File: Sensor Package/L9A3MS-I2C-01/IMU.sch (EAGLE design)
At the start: 15 parts

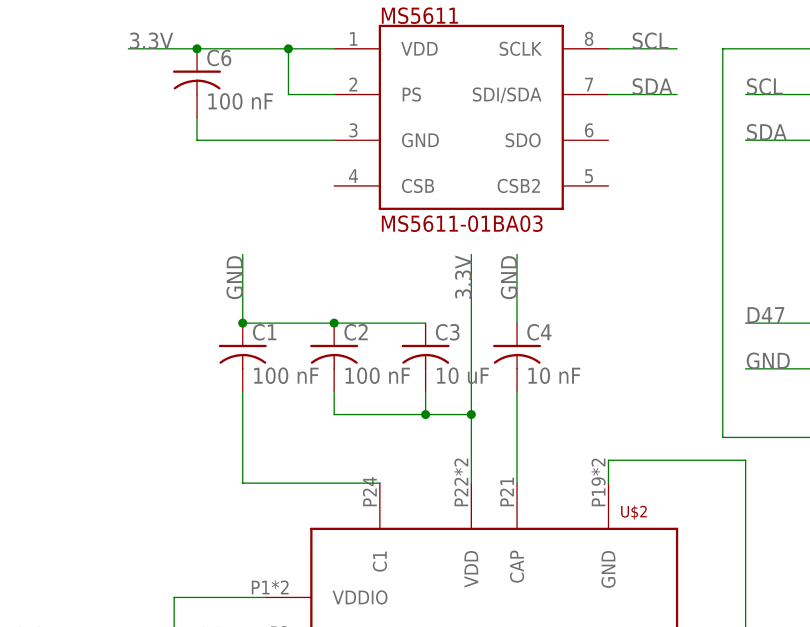
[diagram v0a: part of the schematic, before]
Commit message: Modified Libraries, Worked on STM32F3 Core
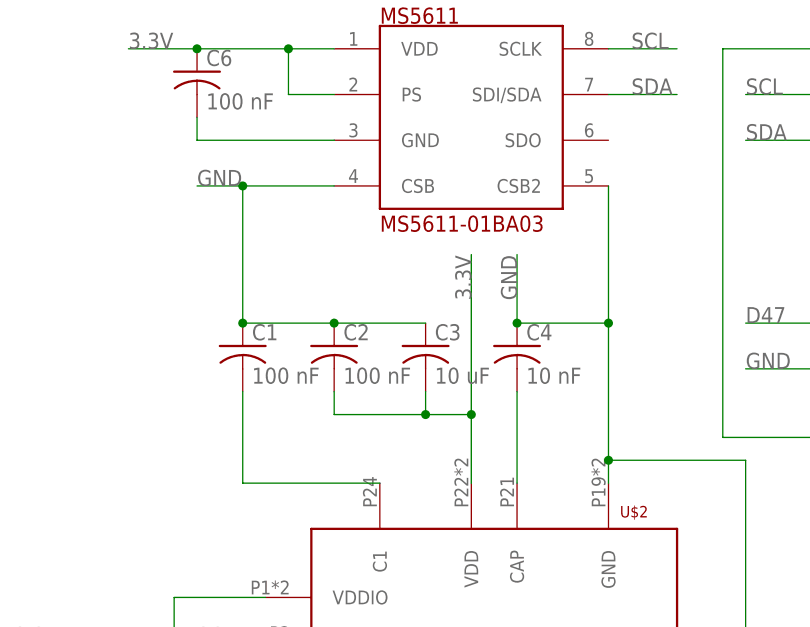
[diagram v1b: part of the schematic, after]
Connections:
- net GND: now also MS5611.CSB, MS5611.CSB2
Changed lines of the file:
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@@
 <?xml version="1.0" encoding="utf-8"?>
 <!DOCTYPE eagle SYSTEM "eagle.dtd">
-<eagle version="8.3.2">
+<eagle version="9.1.1">
 <drawing>
 <settings>
-<setting alwaysvectorfont="no"/>
+<setting alwaysvectorfont="yes"/>
 <setting verticaltext="up"/>
 </settings>
@@
 <pinref part="U$2" gate="G$1" pin="GND"/>
 <pinref part="GND2" gate="1" pin="GND"/>
-</segment>
-<segment>
+<pinref part="MS5611" gate="G$1" pin="CSB2"/>
+<wire x1="109.22" y1="78.74" x2="109.22" y2="63.5" width="0.1524" layer="91"/>
+<junction x="109.22" y="48.26"/>
+<pinref part="C4" gate="G$1" pin="1"/>
+<wire x1="109.22" y1="63.5" x2="109.22" y2="48.26" width="0.1524" layer="91"/>
 <wire x1="99.06" y1="63.5" x2="99.06" y2="71.12" width="0.1524" layer="91"/>
 <label x="99.06" y="66.04" size="1.778" layer="95" rot="R90"/>
-<pinref part="C4" gate="G$1" pin="1"/>
+<wire x1="99.06" y1="63.5" x2="109.22" y2="63.5" width="0.1524" layer="91"/>
+<junction x="99.06" y="63.5"/>
+<junction x="109.22" y="63.5"/>
 </segment>
 <segment>
 <wire x1="88.9" y1="63.5" x2="78.74" y2="63.5" width="0.1524" layer="91"/>
 <wire x1="78.74" y1="63.5" x2="68.58" y2="63.5" width="0.1524" layer="91"/>
-<wire x1="68.58" y1="63.5" x2="68.58" y2="71.12" width="0.1524" layer="91"/>
-<label x="68.58" y="66.04" size="1.778" layer="95" rot="R90"/>
+<label x="63.5" y="78.74" size="1.778" layer="95"/>
 <pinref part="C1" gate="G$1" pin="1"/>
 <junction x="68.58" y="63.5"/>
@@
 <junction x="78.74" y="63.5"/>
 <pinref part="C3" gate="G$1" pin="1"/>
-</segment>
-<segment>
+<pinref part="MS5611" gate="G$1" pin="CSB"/>
+<wire x1="78.74" y1="78.74" x2="68.58" y2="78.74" width="0.1524" layer="91"/>
+<wire x1="68.58" y1="78.74" x2="68.58" y2="63.5" width="0.1524" layer="91"/>
+<wire x1="68.58" y1="78.74" x2="63.5" y2="78.74" width="0.1524" layer="91"/>
+<junction x="68.58" y="78.74"/>
+</segment>
+<segment>
